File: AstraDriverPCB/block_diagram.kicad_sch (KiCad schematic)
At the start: 14 parts, among them CN1 JST_VH_8PIN_10A_250V

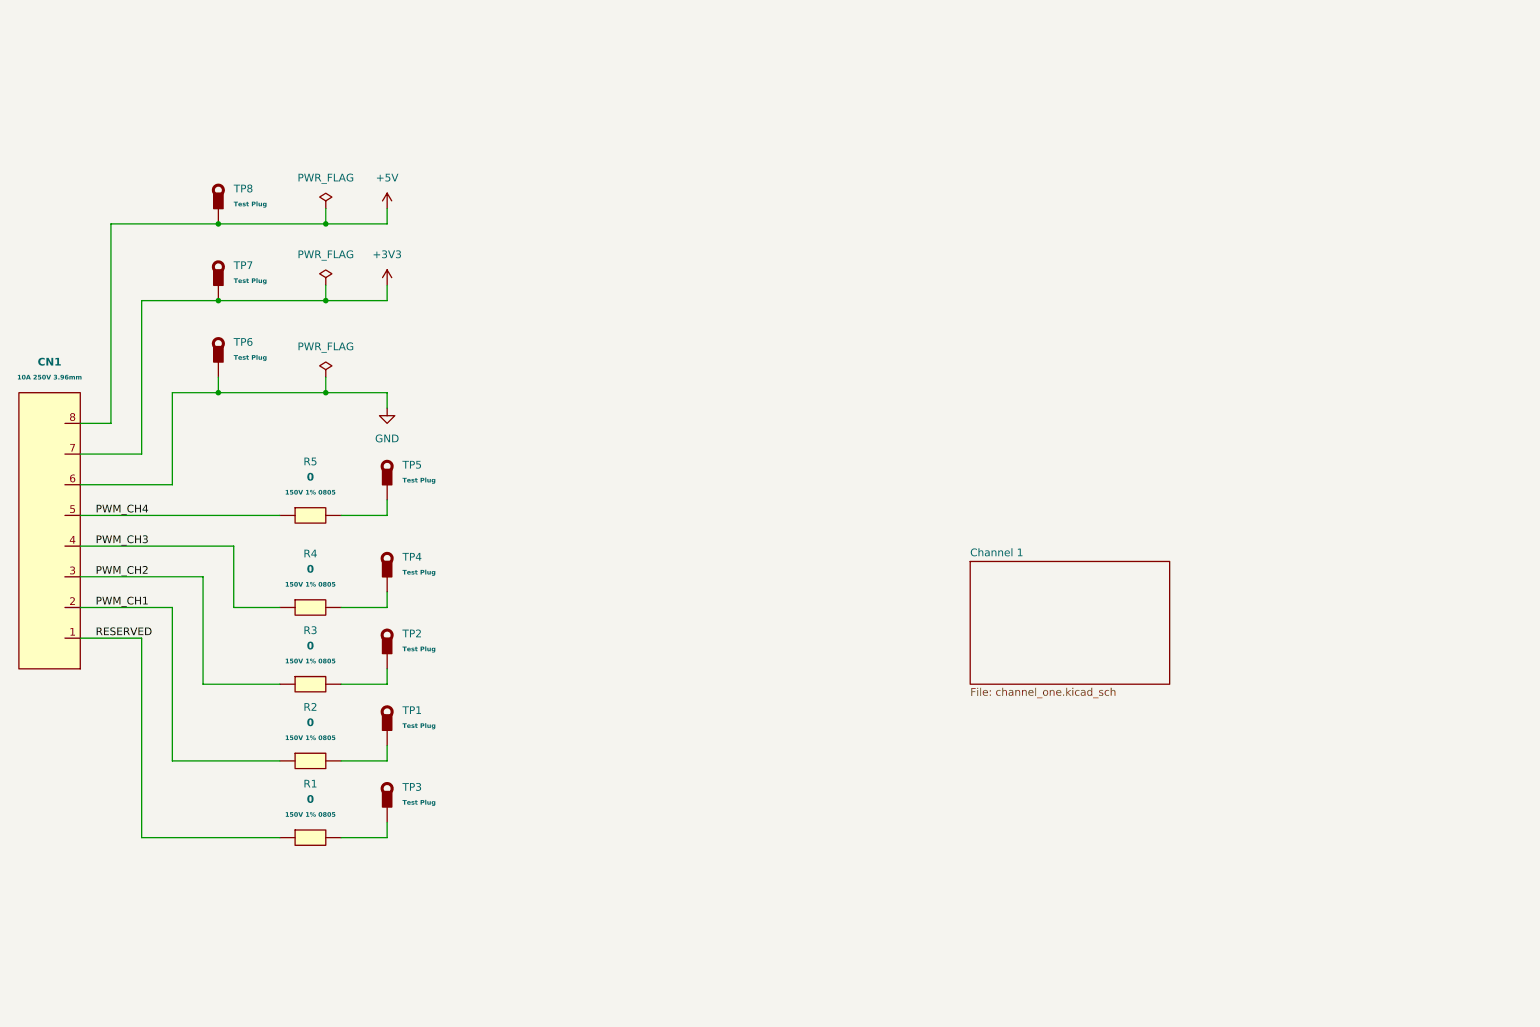
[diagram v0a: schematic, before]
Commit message: Added all schematic components
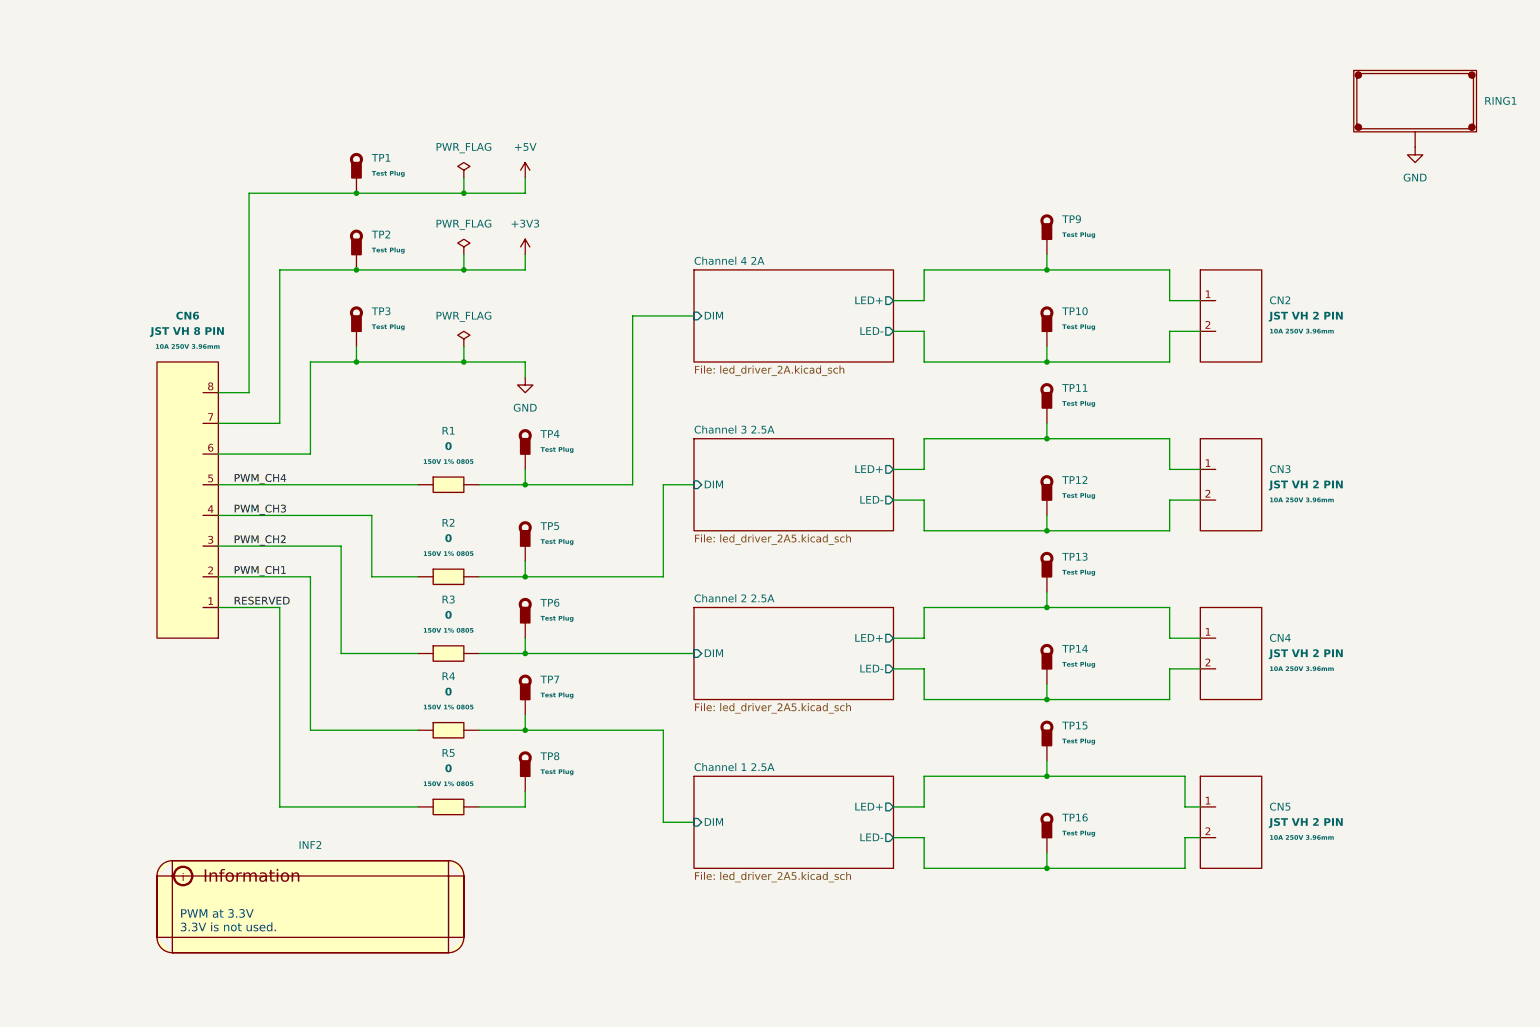
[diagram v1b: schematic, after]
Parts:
- removed CN1: JST_VH_8PIN_10A_250V, LiveAstra:JST_VH_B8P-VH-B_1x08_P3.96mm_Vertical, symbol LiveAstra:JST_VH_8PIN_10A_250V
- added CN2, CN3, CN4, CN5: JST VH 2 PIN, LiveAstra:JST_VH_B2P-VH-B_1x02_P3.96mm_Vertical, symbol LiveAstra:JST_VH_2PIN_10A_250V
- added CN6: JST VH 8 PIN, LiveAstra:JST_VH_B8P-VH-B_1x08_P3.96mm_Vertical, symbol LiveAstra:JST_VH_8PIN_10A_250V
- added INF2: ~, symbol LiveAstra:Information_Box
- added RING1: ~, LiveAstra:AstraControl_Ground_Ring, symbol LiveAstra:AstraControl_Ground_Ring
- added TP10, TP11, TP12, TP13, TP14, TP15, TP16, TP9: TestPoint_Thimble, LiveAstra:TestPoint_Loop_D3.50mm_Drill0.9mm_Beaded, symbol LiveAstra:TestPoint_Thimble
- renumbered R5 to R1, R4 to R2, R2 to R4, R1 to R5, TP8 to TP1, TP7 to TP2, TP6 to TP3, TP5 to TP4, TP4 to TP5, TP2 to TP6, TP1 to TP7, TP3 to TP8
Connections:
- net +3V3: now also CN6.7
- net +5V: now also CN6.8
- net GND: now also CN6.6, RING1.1 (2)
- net PWM_CH1: now also CN6.2
- net PWM_CH2: now also CN6.3
- net PWM_CH3: now also CN6.4
- net PWM_CH4: now also CN6.5
- net RESERVED: now also CN6.1
- net Channel 4 2A/DIM: now reaches R1.2, TP4.1
- net Channel 1 2.5A/DIM: now reaches R4.2, TP7.1
- net Channel 3 2.5A/DIM: now reaches R2.2, TP5.1
- net Channel 2 2.5A/DIM: now reaches R3.2, TP6.1
- new net Channel 1 2.5A/LED+: CN5.1, TP15.1
- new net Channel 1 2.5A/LED-: CN5.2, TP16.1
- new net Channel 2 2.5A/LED+: CN4.1, TP13.1
- new net Channel 2 2.5A/LED-: CN4.2, TP14.1
- new net Channel 3 2.5A/LED+: CN3.1, TP11.1
- new net Channel 3 2.5A/LED-: CN3.2, TP12.1
- new net Channel 4 2A/LED+: CN2.1, TP9.1
- new net Channel 4 2A/LED-: CN2.2, TP10.1
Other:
- sheet Channel 1 renamed Channel 1 2.5A
- added sheet Channel 2 2.5A (led_driver_2A5.kicad_sch)
- added sheet Channel 3 2.5A (led_driver_2A5.kicad_sch)
- added sheet Channel 4 2A (led_driver_2A.kicad_sch)
- sheet Channel 1 2.5A: file channel_one.kicad_sch -> led_driver_2A5.kicad_sch
- sheet Channel 1 2.5A ports: added DIM, LED+, LED-; removed none
- note added: "PWM at 3.3V 3.3V is not used."
- moved on the sheet: R1, R2, R3, R4, R5, TP1, TP2, TP3, TP4, TP5, TP6, TP7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

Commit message: progress
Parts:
- added WRN2: ~, symbol LiveAstra:Warning_Box
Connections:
- net Channel 2 2.5A/LED- is gone; now on net CH2_LED+: CN4.2, TP14.1
- net Channel 3 2.5A/LED- is gone; now on net CH3_LED+: CN3.2, TP12.1
- net Channel 4 2A/LED- is gone; now on net CH4_LED+: CN2.2, TP10.1
- net +3V3: now also CN6.2; no longer CN6.7
- net +5V: now also CN6.1; no longer CN6.8
- net GND: now also CN6.3; no longer CN6.6
- net PWM_CH1: now also CN6.7; no longer CN6.2
- net PWM_CH2: now also CN6.6; no longer CN6.3
- net PWM_CH3: now also CN6.5; no longer CN6.4
- net PWM_CH4: now also CN6.4; no longer CN6.5
- net RESERVED: now also CN6.8; no longer CN6.1
- net RSRV: now reaches R5.2, TP8.1
- net Channel 1 2.5A/DIM renamed DIM_1
- net Channel 1 2.5A/LED+ renamed CH1_LED+
- net Channel 1 2.5A/LED- renamed CH1_LED-
- net Channel 2 2.5A/DIM renamed DIM_2
- net Channel 2 2.5A/LED+ renamed CH2_LED+
- net Channel 3 2.5A/DIM renamed DIM_3
- net Channel 3 2.5A/LED+ renamed CH3_LED+
- net Channel 4 2A/DIM renamed DIM_4
- net Channel 4 2A/LED+ renamed CH4_LED+
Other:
- note added: "Channel 4 is 2.7V 2A. For red LED. The rest are 3.5V 2.5A."
- note added: "PWM at 3.3V 3.3V and RESERVED are not used."
- note removed: "PWM at 3.3V 3.3V is not used."
- moved on the sheet: CN6

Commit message: Finished layout
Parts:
- added R10: 0, LiveAstra:R_0805_2012Metric_Pad1.20x1.40mm_HandSolder, symbol LiveAstra:R_0Ohm_0805_125mW
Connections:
- net +3V3: now also R10.2; no longer CN6.2
- net CH1_LED+: now also CN5.2, TP16.1; no longer CN5.1, TP15.1
- net CH1_LED-: now also CN5.1, TP15.1; no longer CN5.2, TP16.1
- net CH2_LED+: no longer CN4.1, TP13.1
- net CH3_LED+: no longer CN3.1, TP11.1
- net CH4_LED+: no longer CN2.1, TP9.1
- new net 3V3_R: CN6.2, R10.1
- new net CH2_LED-: CN4.1, TP13.1
- new net CH3_LED-: CN3.1, TP11.1
- new net CH4_LED-: CN2.1, TP9.1
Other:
- moved on the sheet: RING1, TP1, TP2, TP3

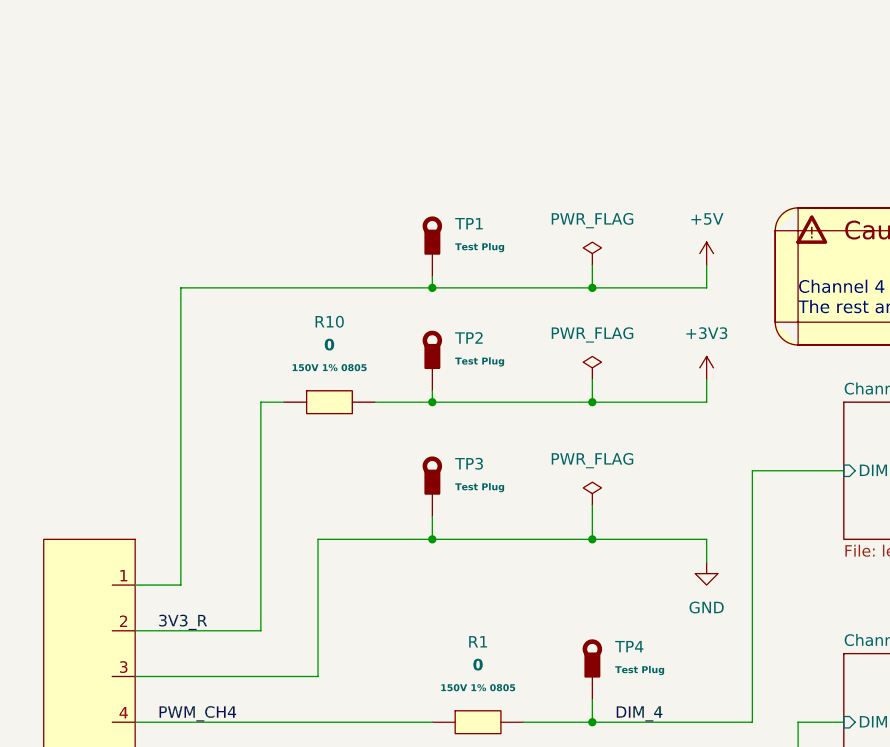
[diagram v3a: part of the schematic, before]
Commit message: Added extra caps, cleanup
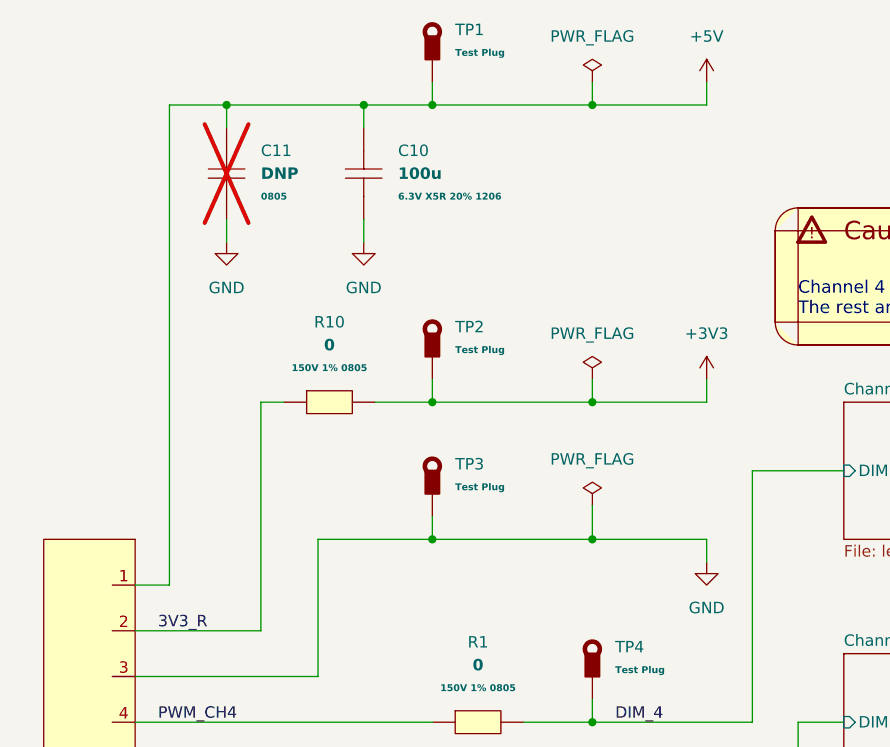
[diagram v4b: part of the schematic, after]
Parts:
- added C10: 100u, LiveAstra:C_1206_3216Metric_Pad1.33x1.80mm_HandSolder, symbol LiveAstra:C_100uF_X5R_1206
- added C11: DNP, LiveAstra:C_DNP_0805_2012Metric_Pad1.18x1.45mm_HandSolder, symbol LiveAstra:C_DNP_0805
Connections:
- net +5V: now also C10.2, C11.2
- net GND: now also C10.1, C11.1
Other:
- moved on the sheet: TP1, TP2

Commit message: Finished silkscreen and board
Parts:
- renumbered C11 to C1, C10 to C2, CN6 to CN1, R10 to R1, R1 to R2, R2 to R3, R3 to R4, R4 to R5, R5 to R6
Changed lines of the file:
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@@
 		(dnp no)
 		(fields_autoplaced yes)
-		(property "Reference" "#PWR040"
+		(property "Reference" "#PWR06"
 			(at 254 58.42 0)
 			(effects
@@
 			(project "AstraDriver"
 				(path "/d8760d88-6646-4dd8-a980-02e776803cc5/db9d16fd-00a9-4695-9dd4-6de80f9e2ffc"
-					(reference "#PWR040")
+					(reference "#PWR06")
 					(unit 1)
 				)
@@
 		(dnp no)
 		(fields_autoplaced yes)
-		(property "Reference" "C10"
+		(property "Reference" "C2"
 			(at 85.09 30.4799 90)
 			(effects
@@
 			(project ""
 				(path "/d8760d88-6646-4dd8-a980-02e776803cc5/db9d16fd-00a9-4695-9dd4-6de80f9e2ffc"
-					(reference "C10")
+					(reference "C2")
 					(unit 1)
 				)
@@
 		(dnp no)
 		(fields_autoplaced yes)
-		(property "Reference" "#PWR01"
+		(property "Reference" "#PWR03"
 			(at 119.38 26.67 0)
 			(effects
@@
 			(project ""
 				(path "/d8760d88-6646-4dd8-a980-02e776803cc5/db9d16fd-00a9-4695-9dd4-6de80f9e2ffc"
-					(reference "#PWR01")
+					(reference "#PWR03")
 					(unit 1)
 				)
@@
 		(dnp no)
 		(fields_autoplaced yes)
-		(property "Reference" "#PWR02"
+		(property "Reference" "#PWR04"
 			(at 119.38 59.69 0)
 			(effects
@@
 			(project ""
 				(path "/d8760d88-6646-4dd8-a980-02e776803cc5/db9d16fd-00a9-4695-9dd4-6de80f9e2ffc"
-					(reference "#PWR02")
+					(reference "#PWR04")
 					(unit 1)
 				)
@@
 		(dnp no)
 		(fields_autoplaced yes)
-		(property "Reference" "R10"
+		(property "Reference" "R1"
 			(at 77.47 49.53 0)
 			(effects
@@
 			(project "AstraDriver"
 				(path "/d8760d88-6646-4dd8-a980-02e776803cc5/db9d16fd-00a9-4695-9dd4-6de80f9e2ffc"
-					(reference "R10")
+					(reference "R1")
 					(unit 1)
 				)
@@
 		(dnp no)
 		(fields_autoplaced yes)
-		(property "Reference" "#PWR03"
+		(property "Reference" "#PWR05"
 			(at 119.38 82.55 0)
 			(effects
@@
 			(project ""
 				(path "/d8760d88-6646-4dd8-a980-02e776803cc5/db9d16fd-00a9-4695-9dd4-6de80f9e2ffc"
-					(reference "#PWR03")
+					(reference "#PWR05")
 					(unit 1)
 				)
@@
 		(dnp no)
 		(fields_autoplaced yes)
-		(property "Reference" "R1"
+		(property "Reference" "R2"
 			(at 93.98 85.09 0)
 			(effects
@@
 			(project "AstraDriver"
 				(path "/d8760d88-6646-4dd8-a980-02e776803cc5/db9d16fd-00a9-4695-9dd4-6de80f9e2ffc"
-					(reference "R1")
+					(reference "R2")
 					(unit 1)
 				)
@@
 		(dnp no)
 		(fields_autoplaced yes)
-		(property "Reference" "R4"
+		(property "Reference" "R5"
 			(at 93.98 125.73 0)
 			(effects
@@
 			(project "AstraDriver"
 				(path "/d8760d88-6646-4dd8-a980-02e776803cc5/db9d16fd-00a9-4695-9dd4-6de80f9e2ffc"
-					(reference "R4")
+					(reference "R5")
 					(unit 1)
 				)
@@
 		(dnp no)
 		(fields_autoplaced yes)
-		(property "Reference" "R2"
+		(property "Reference" "R3"
 			(at 93.98 100.33 0)
 			(effects
@@
 			(project "AstraDriver"
 				(path "/d8760d88-6646-4dd8-a980-02e776803cc5/db9d16fd-00a9-4695-9dd4-6de80f9e2ffc"
-					(reference "R2")
+					(reference "R3")
 					(unit 1)
 				)
@@
 		(dnp yes)
 		(fields_autoplaced yes)
-		(property "Reference" "C11"
+		(property "Reference" "C1"
 			(at 69.85 30.4799 90)
 			(effects
@@
 			(project ""
 				(path "/d8760d88-6646-4dd8-a980-02e776803cc5/db9d16fd-00a9-4695-9dd4-6de80f9e2ffc"
-					(reference "C11")
+					(reference "C1")
 					(unit 1)
 				)
@@
 		(dnp no)
 		(fields_autoplaced yes)
-		(property "Reference" "R3"
+		(property "Reference" "R4"
 			(at 93.98 113.03 0)
 			(effects
@@
 			(project "AstraDriver"
 				(path "/d8760d88-6646-4dd8-a980-02e776803cc5/db9d16fd-00a9-4695-9dd4-6de80f9e2ffc"
-					(reference "R3")
+					(reference "R4")
 					(unit 1)
 				)
@@
 		(dnp no)
 		(fields_autoplaced yes)
-		(property "Reference" "#PWR042"
+		(property "Reference" "#PWR01"
 			(at 66.04 46.99 0)
 			(effects
@@
 			(project "AstraDriver"
 				(path "/d8760d88-6646-4dd8-a980-02e776803cc5/db9d16fd-00a9-4695-9dd4-6de80f9e2ffc"
-					(reference "#PWR042")
+					(reference "#PWR01")
 					(unit 1)
 				)
@@
 		(dnp no)
 		(fields_autoplaced yes)
-		(property "Reference" "#PWR041"
+		(property "Reference" "#PWR02"
 			(at 81.28 46.99 0)
 			(effects
@@
 			(project "AstraDriver"
 				(path "/d8760d88-6646-4dd8-a980-02e776803cc5/db9d16fd-00a9-4695-9dd4-6de80f9e2ffc"
-					(reference "#PWR041")
+					(reference "#PWR02")
 					(unit 1)
 				)
@@
 		(on_board yes)
 		(dnp no)
-		(property "Reference" "CN6"
+		(property "Reference" "CN1"
 			(at 50.8 127 0)
 			(effects
@@
 			(project ""
 				(path "/d8760d88-6646-4dd8-a980-02e776803cc5/db9d16fd-00a9-4695-9dd4-6de80f9e2ffc"
-					(reference "CN6")
+					(reference "CN1")
 					(unit 1)
 				)
@@
 		(dnp no)
 		(fields_autoplaced yes)
-		(property "Reference" "R5"
+		(property "Reference" "R6"
 			(at 93.98 138.43 0)
 			(effects
@@
 			(project "AstraDriver"
 				(path "/d8760d88-6646-4dd8-a980-02e776803cc5/db9d16fd-00a9-4695-9dd4-6de80f9e2ffc"
-					(reference "R5")
+					(reference "R6")
 					(unit 1)
 				)

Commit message: New layout in progress
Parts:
- removed INF2: ~, symbol LiveAstra:Information_Box
- removed RING1: ~, LiveAstra:AstraControl_Ground_Ring, symbol LiveAstra:AstraControl_Ground_Ring
- added R15, R16, R17, R18, R19: 10k, LiveAstra:R_0805_2012Metric_Pad1.20x1.40mm_HandSolder, symbol LiveAstra:R_10kOhm_0805_125mW
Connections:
- net DIM_1: now also R16.2
- net DIM_2: now also R19.2
- net DIM_3: now also R18.2
- net DIM_4: now also R17.2
- net GND: now also R15.1, R16.1, R17.1, R18.1, R19.1
- net RSRV: now also R15.2
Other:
- sheet Channel 2 2.5A renamed Channel 2 Blue and CY 2.5A
- sheet Channel 3 2.5A renamed Channel 3 Green 2.5A
- sheet Channel 4 2A renamed Channel 4 Red 2A
- removed sheet Channel 1 2.5A
- added sheet Channel 1 Blue and CY 2.5A (led_driver_blue_cy_2A5.kicad_sch)
- added sheet Misc (misc.kicad_sch)
- sheet Channel 2 Blue and CY 2.5A: file led_driver_2A5.kicad_sch -> led_driver_blue_cy_2A5.kicad_sch
- sheet Channel 3 Green 2.5A: file led_driver_2A5.kicad_sch -> led_driver_green_2A5.kicad_sch
- sheet Channel 4 Red 2A: file led_driver_2A.kicad_sch -> led_driver_red_2A.kicad_sch
- note added: "Channel 4 is 2A, For red LED. The rest are 2.5A."
- note removed: "Channel 4 is 2.7V 2A. For red LED. The rest are 3.5V 2.5A."
- note removed: "PWM at 3.3V 3.3V and RESERVED are not used."
- moved on the sheet: C1, C2, CN1, R1, R2, R3, R4, R5, R6, TP2, TP3, TP4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

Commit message: Prepare for review, cleanup
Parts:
- renumbered R6 to R1, R19 to R10, R16 to R11, R15 to R2, R1 to R3, R2 to R4, R3 to R5, R4 to R6, R5 to R7, R17 to R8, R18 to R9, TP3 to TP1, TP8 to TP2, TP1 to TP3, TP2 to TP4, TP4 to TP5, TP5 to TP6, TP6 to TP7, TP7 to TP8
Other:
- moved on the sheet: CN1

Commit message: Cleanup
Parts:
- added INF2: ~, symbol LiveAstra:Information_Box
- renumbered R4 to R1, R5 to R2, R6 to R3, R7 to R4, R1 to R5, R3 to R6, R2 to R7
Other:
- note added: "10k pull down resistors to keep DIM LOW while the controller is booting or offline."
- moved on the sheet: CN1, R1, R2, R3, R4, R5, R7, TP2, TP5
